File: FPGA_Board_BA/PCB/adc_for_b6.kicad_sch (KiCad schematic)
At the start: 17 parts, among them U1 LTC2320-16_CMOS

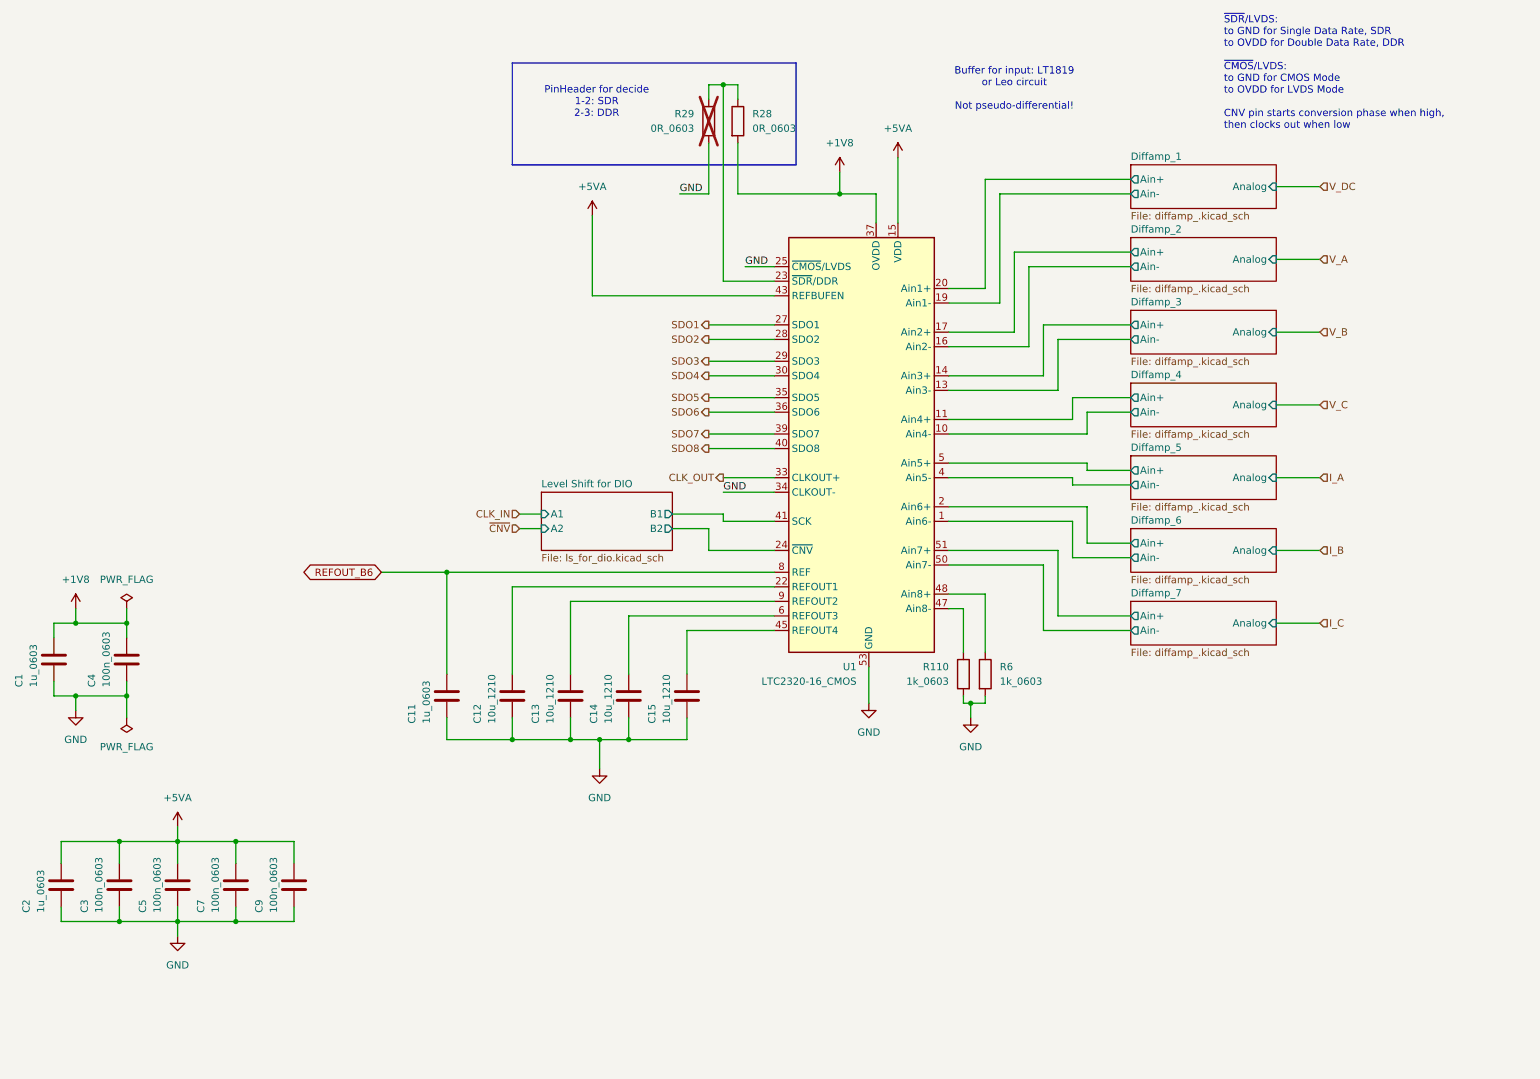
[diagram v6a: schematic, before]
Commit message: big schematic cleanup. Added wire to bus
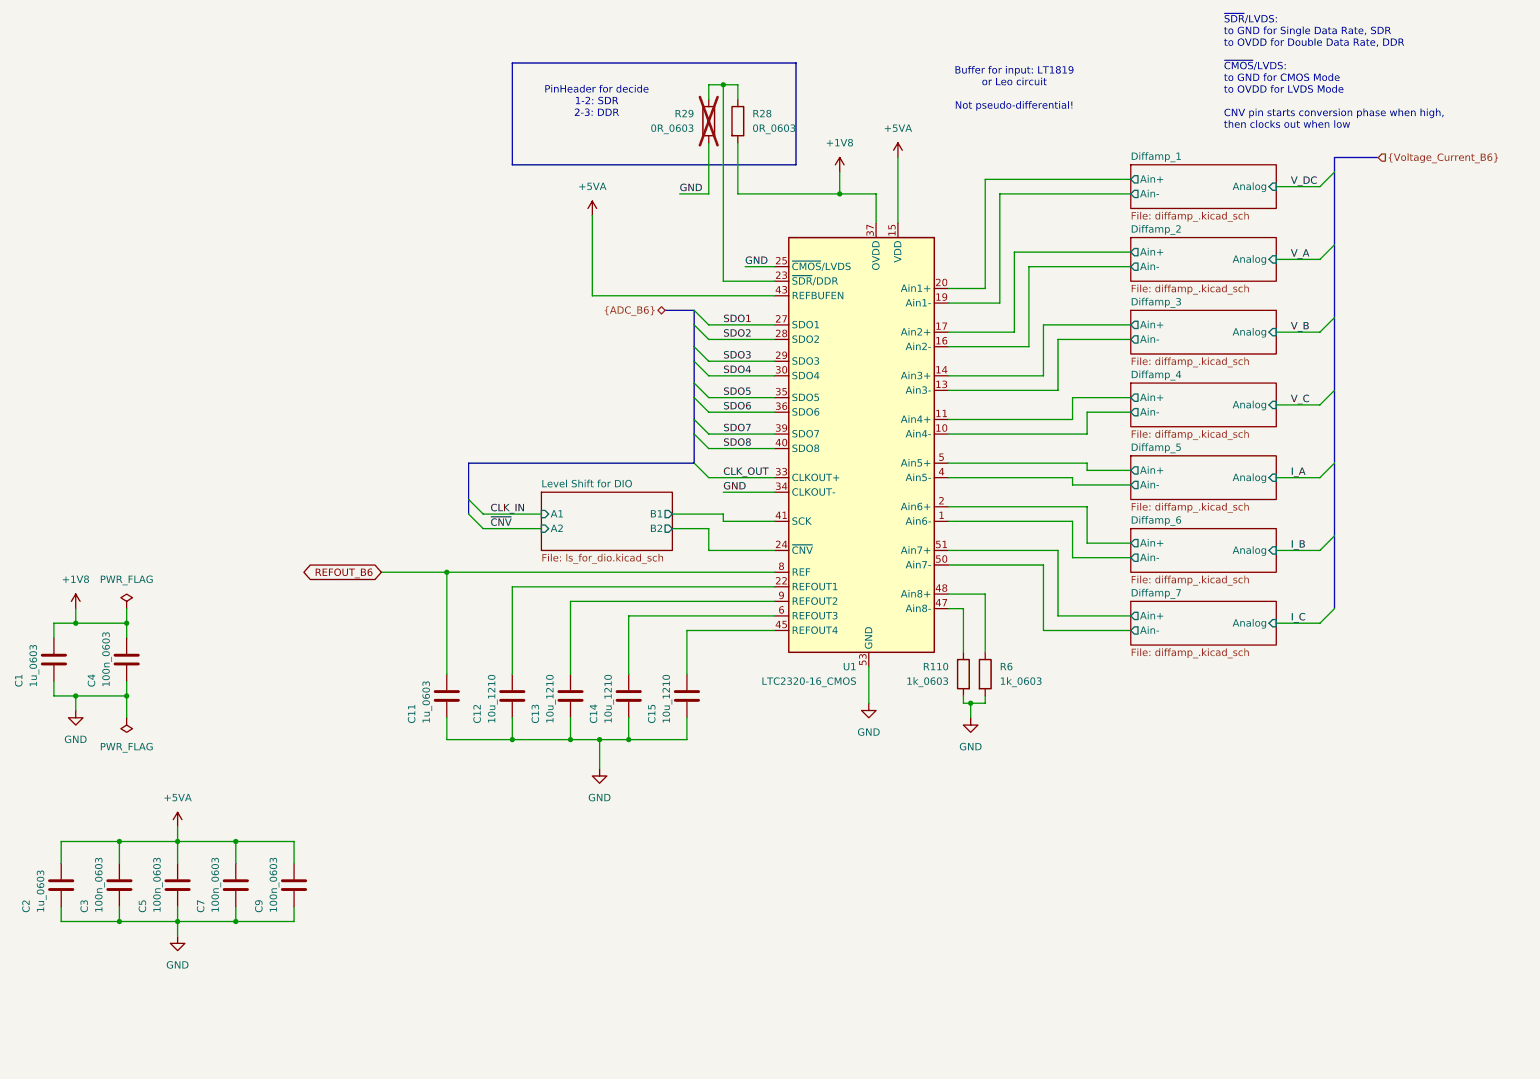
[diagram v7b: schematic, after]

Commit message: PCB left side almost finished + some optimization in schematics
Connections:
- net Diffamp_1/Ain+: now also U1.51 (Ain7+); no longer U1.20 (Ain1+)
- net Diffamp_1/Ain-: now also U1.50 (Ain7-); no longer U1.19 (Ain1-)
- net Diffamp_2/Ain+: now also U1.14 (Ain3+); no longer U1.17 (Ain2+)
- net Diffamp_2/Ain-: now also U1.13 (Ain3-); no longer U1.16 (Ain2-)
- net Diffamp_3/Ain+: now also U1.2 (Ain6+); no longer U1.14 (Ain3+)
- net Diffamp_3/Ain-: now also U1.1 (Ain6-); no longer U1.13 (Ain3-)
- net Diffamp_4/Ain+: now also U1.17 (Ain2+); no longer U1.11 (Ain4+)
- net Diffamp_4/Ain-: now also U1.16 (Ain2-); no longer U1.10 (Ain4-)
- net Diffamp_6/Ain+: now also U1.20 (Ain1+); no longer U1.2 (Ain6+)
- net Diffamp_6/Ain-: now also U1.19 (Ain1-); no longer U1.1 (Ain6-)
- net Diffamp_7/Ain+: now also U1.11 (Ain4+); no longer U1.51 (Ain7+)
- net Diffamp_7/Ain-: now also U1.10 (Ain4-); no longer U1.50 (Ain7-)
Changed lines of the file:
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@@
 		)
 	)
+	(bus_alias "Voltage_Current_B6"
+		(members "V_DC" "V_A" "V_B" "V_C" "I_A" "I_B" "I_C")
+	)
 	(rectangle
 		(start 107.95 21.59)
@@
 	(wire
 		(pts
-			(xy 241.3 119.38) (xy 248.92 119.38)
+			(xy 241.3 81.28) (xy 248.92 81.28)
 		)
 		(stroke
@@
 	(wire
 		(pts
+			(xy 193.04 44.45) (xy 215.9 44.45)
+		)
+		(stroke
+			(width 0)
+			(type default)
+		)
+	)
+	(wire
+		(pts
 			(xy 153.67 115.57) (xy 118.11 115.57)
 		)
@@
 	(wire
 		(pts
-			(xy 241.3 68.58) (xy 248.92 68.58)
+			(xy 241.3 106.68) (xy 248.92 106.68)
 		)
 		(stroke
@@
 	(wire
 		(pts
-			(xy 241.3 81.28) (xy 248.92 81.28)
+			(xy 241.3 55.88) (xy 248.92 55.88)
 		)
 		(stroke
@@
 	(wire
 		(pts
-			(xy 241.3 106.68) (xy 248.92 106.68)
+			(xy 241.3 43.18) (xy 248.92 43.18)
 		)
 		(stroke
@@
 	(wire
 		(pts
-			(xy 241.3 55.88) (xy 248.92 55.88)
+			(xy 241.3 68.58) (xy 248.92 68.58)
 		)
 		(stroke
@@
 	(wire
 		(pts
-			(xy 241.3 43.18) (xy 248.92 43.18)
+			(xy 241.3 119.38) (xy 248.92 119.38)
 		)
 		(stroke
@@
 		)
 	)
-	(wire
-		(pts
-			(xy 215.9 44.45) (xy 193.04 44.45)
-		)
-		(stroke
-			(width 0)
-			(type default)
-		)
-	)
 	(bus
 		(pts
@@
 	)
 	(label "V_DC"
-		(at 243.84 43.18 0)
+		(at 243.84 119.38 0)
 		(effects
 			(font
@@
 	)
 	(label "V_A"
-		(at 243.84 55.88 0)
+		(at 243.84 68.58 0)
 		(effects
 			(font
@@
 	)
 	(label "I_C"
-		(at 243.84 119.38 0)
+		(at 243.84 81.28 0)
 		(effects
 			(font
@@
 	)
 	(label "V_C"
-		(at 243.84 81.28 0)
+		(at 243.84 55.88 0)
 		(effects
 			(font
@@
 	)
 	(label "V_B"
-		(at 243.84 68.58 0)
+		(at 243.84 106.68 0)
 		(effects
 			(font
@@
 	)
 	(label "I_B"
-		(at 243.84 106.68 0)
+		(at 243.84 43.18 0)
 		(effects
 			(font
@@
 	)
 	(sheet
-		(at 215.9 102.87)
+		(at 215.9 39.37)
 		(size 25.4 7.62)
 		(exclude_from_sim no)
@@
 		)
 		(property "Sheetname" "Diffamp_6"
-			(at 215.9 102.1584 0)
+			(at 215.9 38.6584 0)
 			(effects
 				(font
@@
 		)
 		(property "Sheetfile" "diffamp_.kicad_sch"
-			(at 215.9 111.0746 0)
+			(at 215.9 47.5746 0)
 			(effects
 				(font
@@
 		)
 		(pin "Ain+" output
-			(at 215.9 105.41 180)
+			(at 215.9 41.91 180)
 			(effects
 				(font
@@
 		)
 		(pin "Ain-" output
-			(at 215.9 107.95 180)
+			(at 215.9 44.45 180)
 			(effects
 				(font
@@
 		)
 		(pin "Analog" input
-			(at 241.3 106.68 0)
+			(at 241.3 43.18 0)
 			(effects
 				(font
@@
 	)
 	(sheet
-		(at 215.9 77.47)
+		(at 215.9 52.07)
 		(size 25.4 7.62)
 		(exclude_from_sim no)
@@
 		)
 		(property "Sheetname" "Diffamp_4"
-			(at 215.9 76.7584 0)
+			(at 215.9 51.3584 0)
 			(effects
 				(font
@@
 		)
 		(property "Sheetfile" "diffamp_.kicad_sch"
-			(at 215.9 85.6746 0)
+			(at 215.9 60.2746 0)
 			(effects
 				(font
@@
 		)
 		(pin "Ain+" output
-			(at 215.9 80.01 180)
+			(at 215.9 54.61 180)
 			(effects
 				(font
@@
 		)
 		(pin "Ain-" output
-			(at 215.9 82.55 180)
+			(at 215.9 57.15 180)
 			(effects
 				(font
@@
 		)
 		(pin "Analog" input
-			(at 241.3 81.28 0)
+			(at 241.3 55.88 0)
 			(effects
 				(font
@@
 	)
 	(sheet
-		(at 215.9 115.57)
+		(at 215.9 77.47)
 		(size 25.4 7.62)
 		(exclude_from_sim no)
@@
 		)
 		(property "Sheetname" "Diffamp_7"
-			(at 215.9 114.8584 0)
+			(at 215.9 76.7584 0)
 			(effects
 				(font
@@
 		)
 		(property "Sheetfile" "diffamp_.kicad_sch"
-			(at 215.9 123.7746 0)
+			(at 215.9 85.6746 0)
 			(effects
 				(font
@@
 		)
 		(pin "Ain+" output
-			(at 215.9 118.11 180)
+			(at 215.9 80.01 180)
 			(effects
 				(font
@@
 		)
 		(pin "Ain-" output
-			(at 215.9 120.65 180)
+			(at 215.9 82.55 180)
 			(effects
 				(font
@@
 		)
 		(pin "Analog" input
-			(at 241.3 119.38 0)
+			(at 241.3 81.28 0)
 			(effects
 				(font
@@
 	)
 	(sheet
-		(at 215.9 39.37)
+		(at 215.9 115.57)
 		(size 25.4 7.62)
 		(exclude_from_sim no)
@@
 		)
 		(property "Sheetname" "Diffamp_1"
-			(at 215.9 38.6584 0)
+			(at 215.9 114.8584 0)
 			(effects
 				(font
@@
 		)
 		(property "Sheetfile" "diffamp_.kicad_sch"
-			(at 215.9 47.5746 0)
+			(at 215.9 123.7746 0)
 			(effects
 				(font
@@
 		)
 		(pin "Ain+" output
-			(at 215.9 41.91 180)
+			(at 215.9 118.11 180)
 			(effects
 				(font
@@
 		)
 		(pin "Ain-" output
-			(at 215.9 44.45 180)
+			(at 215.9 120.65 180)
 			(effects
 				(font
@@
 		)
 		(pin "Analog" input
-			(at 241.3 43.18 0)
+			(at 241.3 119.38 0)
 			(effects
 				(font
@@
 	)
 	(sheet
-		(at 215.9 64.77)
+		(at 215.9 102.87)
 		(size 25.4 7.62)
 		(exclude_from_sim no)
@@
 		)
 		(property "Sheetname" "Diffamp_3"
-			(at 215.9 64.0584 0)
+			(at 215.9 102.1584 0)
 			(effects
 				(font
@@
 		)
 		(property "Sheetfile" "diffamp_.kicad_sch"
-			(at 215.9 72.9746 0)
+			(at 215.9 111.0746 0)
 			(effects
 				(font
@@
 		)
 		(pin "Ain+" output
-			(at 215.9 67.31 180)
+			(at 215.9 105.41 180)
 			(effects
 				(font
@@
 		)
 		(pin "Ain-" output
-			(at 215.9 69.85 180)
+			(at 215.9 107.95 180)
 			(effects
 				(font
@@
 		)
 		(pin "Analog" input
-			(at 241.3 68.58 0)
+			(at 241.3 106.68 0)
 			(effects
 				(font
@@
 	)
 	(sheet
-		(at 215.9 52.07)
+		(at 215.9 64.77)
 		(size 25.4 7.62)
 		(exclude_from_sim no)
@@
 		)
 		(property "Sheetname" "Diffamp_2"
-			(at 215.9 51.3584 0)
+			(at 215.9 64.0584 0)
 			(effects
 				(font
@@
 		)
 		(property "Sheetfile" "diffamp_.kicad_sch"
-			(at 215.9 60.2746 0)
+			(at 215.9 72.9746 0)
 			(effects
 				(font
@@
 		)
 		(pin "Ain+" output
-			(at 215.9 54.61 180)
+			(at 215.9 67.31 180)
 			(effects
 				(font
@@
 		)
 		(pin "Ain-" output
-			(at 215.9 57.15 180)
+			(at 215.9 69.85 180)
 			(effects
 				(font
@@
 		)
 		(pin "Analog" input
-			(at 241.3 55.88 0)
+			(at 241.3 68.58 0)
 			(effects
 				(font
